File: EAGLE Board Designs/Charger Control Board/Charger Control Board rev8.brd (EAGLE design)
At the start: 86.4 x 83.8 mm, 121 parts, among them J1 CONNECTOR-4_μF_T_V_BLACK, K1 RELAY_DPDT_RT424024, K2 RELAY_DPDT_RT424024, K3 RELAY_DPDT_RT424024, U1 LOGICGATE_BUFFER, U2 ADM8316WBX30, U3 VOLTAGE_REGULATOR_MODULE_OKI-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, U4 TCAN1051HQV-Q1, U5 TCAN1051HQV-Q1

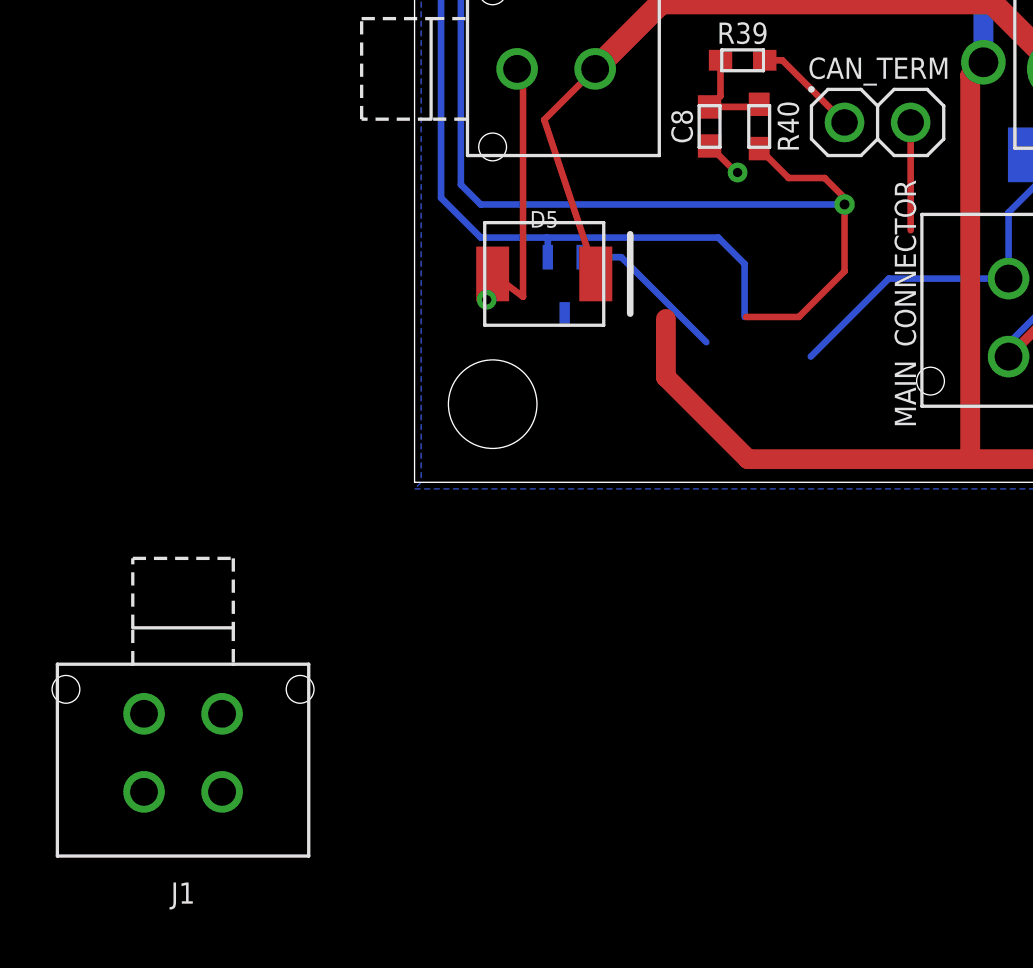
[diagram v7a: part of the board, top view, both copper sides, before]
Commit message: positioning of J1
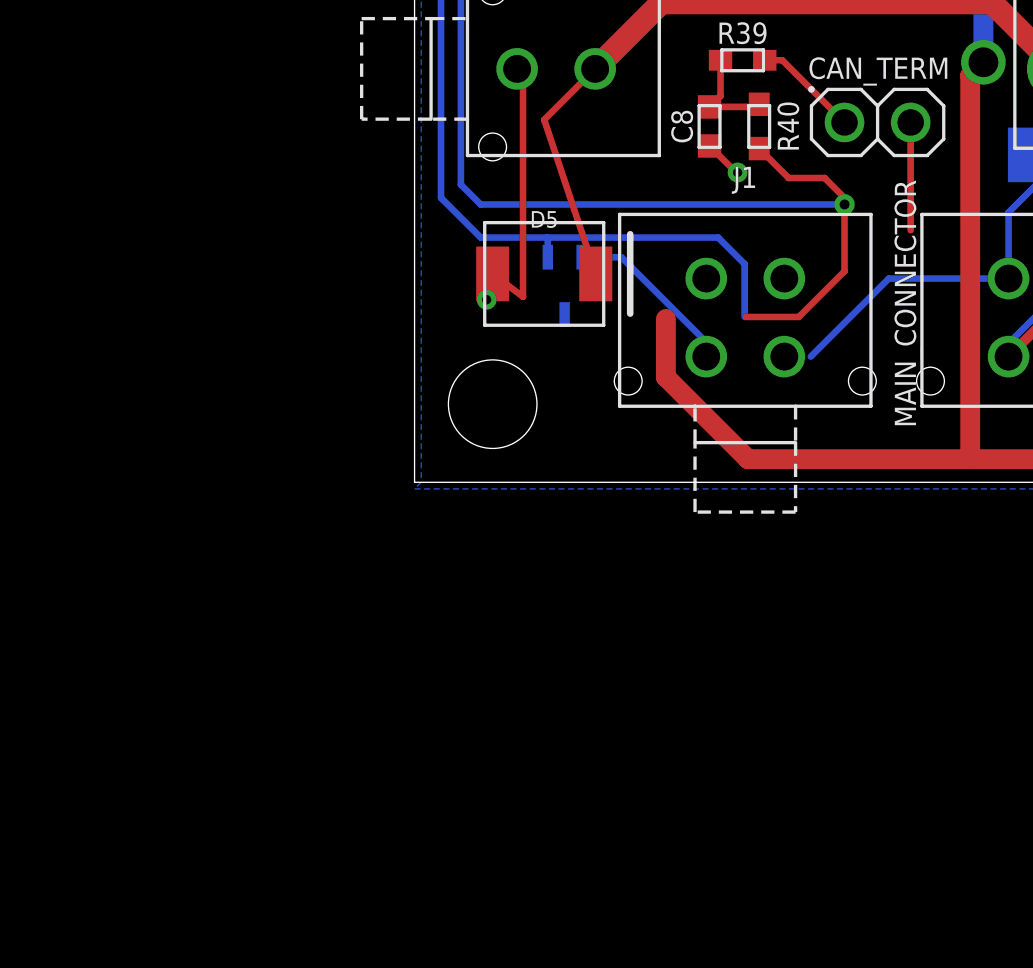
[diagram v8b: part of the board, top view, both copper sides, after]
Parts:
- moved J1 25.6 mm to (12.7, 4.83), turned to 180 degrees
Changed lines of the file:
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@@
 <attribute name="NAME" x="16.383" y="73.787" size="0.8128" layer="25" font="vector" rot="R90" align="bottom-center"/>
 </element>
-<element name="J1" library="HyTechDevices" package="MOLEX_MICROFIT_PTH_VERTICAL_04_DUAL" value="CONNECTOR-4_μF_T_V_BLACK" x="-8.89" y="-8.89" smashed="yes">
-<attribute name="DKPN" value="2266-43045-0414-ND" x="-8.89" y="-8.89" size="1.778" layer="27" display="off"/>
-<attribute name="MANUFACTURER" value="Molex" x="-8.89" y="-8.89" size="1.778" layer="27" display="off"/>
-<attribute name="MOPN" value="538-43045-0414" x="-8.89" y="-8.89" size="1.778" layer="27" display="off"/>
-<attribute name="MPN" value="430450414" x="-8.89" y="-8.89" size="1.778" layer="27" display="off"/>
-<attribute name="NAME" x="-8.89" y="-15.367" size="0.8128" layer="25" rot="R180" align="bottom-center"/>
+<element name="J1" library="HyTechDevices" package="MOLEX_MICROFIT_PTH_VERTICAL_04_DUAL" value="CONNECTOR-4_μF_T_V_BLACK" x="12.7" y="4.826" smashed="yes" rot="R180">
+<attribute name="DKPN" value="2266-43045-0414-ND" x="12.7" y="4.826" size="1.778" layer="27" rot="R180" display="off"/>
+<attribute name="MANUFACTURER" value="Molex" x="12.7" y="4.826" size="1.778" layer="27" rot="R180" display="off"/>
+<attribute name="MOPN" value="538-43045-0414" x="12.7" y="4.826" size="1.778" layer="27" rot="R180" display="off"/>
+<attribute name="MPN" value="430450414" x="12.7" y="4.826" size="1.778" layer="27" rot="R180" display="off"/>
+<attribute name="NAME" x="12.7" y="11.303" size="0.8128" layer="25" align="bottom-center"/>
 </element>
 </elements>
@@
 <wire x1="5.7658" y1="6.4438" x2="2.7686" y2="7.0104" width="0" layer="19" extent="16-16"/>
 <wire x1="11.3284" y1="12.9152" x2="3.937" y2="15.875" width="0" layer="19" extent="1-1"/>
+<wire x1="14.1986" y1="4.826" x2="12.4042875" y2="11.8962875" width="0" layer="19" extent="1-1"/>
 <wire x1="48.9204" y1="48.6918" x2="52.8442" y2="57.277" width="0" layer="19" extent="1-1"/>
 <wire x1="18.022" y1="69.977" x2="8.89" y2="66.04" width="0" layer="19" extent="16-16"/>
-<wire x1="24.13" y1="71.64" x2="18.022" y2="69.977" width="0" layer="19" extent="16-16"/>
+<wire x1="18.923" y1="71.1835" x2="18.022" y2="69.977" width="0" layer="19" extent="1-16"/>
+<wire x1="24.13" y1="71.64" x2="18.923" y2="71.1835" width="0" layer="19" extent="1-16"/>
+<wire x1="17.653" y1="76.3905" x2="18.923" y2="71.1835" width="0" layer="19" extent="1-1"/>
+<wire x1="11.43" y1="81.28" x2="17.653" y2="76.3905" width="0" layer="19" extent="1-1"/>
 <wire x1="23.42" y1="12.573" x2="12.4042875" y2="11.8962875" width="0" layer="19" extent="16-16"/>
 <wire x1="27.23" y1="12.573" x2="23.42" y2="12.573" width="0" layer="19" extent="16-16"/>
@@
 <wire x1="46.0502" y1="4.826" x2="41.0464" y2="13.3252" width="0" layer="19" extent="16-16"/>
 <wire x1="54.9784" y1="3.1094" x2="46.0502" y2="4.826" width="0" layer="19" extent="1-1"/>
-<wire x1="11.43" y1="81.28" x2="18.022" y2="69.977" width="0" layer="19" extent="16-16"/>
 <wire x1="79.97" y1="34.23" x2="79.97" y2="47.692" width="0" layer="19" extent="1-1"/>
 <wire x1="79.97" y1="20.768" x2="79.97" y2="34.23" width="0" layer="19" extent="1-1"/>
-<wire x1="17.653" y1="76.3905" x2="2.7686" y2="7.0104" width="0" layer="19" extent="1-1"/>
-<wire x1="18.923" y1="71.1835" x2="17.653" y2="76.3905" width="0" layer="19" extent="1-1"/>
-<wire x1="-10.3886" y1="-8.89" x2="17.653" y2="76.3905" width="0" layer="19" extent="1-1"/>
 <wire x1="44.45" y1="81.28" x2="44.9208" y2="59.817" width="0" layer="19" extent="1-1"/>
 </signal>
@@
 <wire x1="39.9386" y1="32.766" x2="37.465" y2="32.766" width="0.381" layer="1"/>
 <contactref element="J1" pad="1"/>
-<wire x1="9.652" y1="6.2738" x2="-7.3914" y2="-11.8872" width="0" layer="19" extent="1-1"/>
+<wire x1="9.652" y1="6.2738" x2="11.2014" y2="7.8232" width="0" layer="19" extent="1-1"/>
 </signal>
 <signal name="+5V">
@@
 <contactref element="U5" pad="6"/>
 <contactref element="J1" pad="3"/>
-<wire x1="15.113" y1="52.959" x2="22.1615" y2="52.959" width="0" layer="19" extent="1-16"/>
+<wire x1="8.2042" y1="73.152" x2="20.193" y2="76.3905" width="0" layer="19" extent="1-16"/>
 <wire x1="11.2014" y1="5.3822" x2="12.7254" y2="6.35" width="0" layer="19" extent="1-16"/>
-<wire x1="15.0518" y1="0.9756" x2="12.7254" y2="6.35" width="0" layer="19" extent="1-16"/>
-<wire x1="20.193" y1="76.3905" x2="15.0518" y2="0.9756" width="0" layer="19" extent="1-16"/>
-<wire x1="-7.3914" y1="-8.89" x2="20.193" y2="76.3905" width="0" layer="19" extent="1-1"/>
+<wire x1="11.2014" y1="4.826" x2="11.2014" y2="5.3822" width="0" layer="19" extent="16-16"/>
+<wire x1="15.0518" y1="0.9756" x2="11.2014" y2="4.826" width="0" layer="19" extent="16-16"/>
+<wire x1="22.1615" y1="52.959" x2="15.113" y2="52.959" width="0" layer="19" extent="1-16"/>
 </signal>
 <signal name="CANH">
@@
 <contactref element="U5" pad="7"/>
 <contactref element="J1" pad="2"/>
-<wire x1="16.8275" y1="54.356" x2="22.1615" y2="54.229" width="0" layer="19" extent="1-16"/>
+<wire x1="8.382" y1="74.422" x2="18.923" y2="76.3905" width="0" layer="19" extent="1-16"/>
+<wire x1="14.1986" y1="7.8232" x2="12.6746" y2="6.35" width="0" layer="19" extent="16-16"/>
 <wire x1="15.2146" y1="4.826" x2="12.6746" y2="6.35" width="0" layer="19" extent="16-16"/>
 <wire x1="19.05" y1="9.6774" x2="22.8092" y2="7.8232" width="0" layer="19" extent="1-1"/>
-<wire x1="18.923" y1="76.3905" x2="5.1158" y2="8.6438" width="0" layer="19" extent="1-16"/>
-<wire x1="-10.3886" y1="-11.8872" x2="18.923" y2="76.3905" width="0" layer="19" extent="1-1"/>
+<wire x1="22.1615" y1="54.229" x2="16.8275" y2="54.356" width="0" layer="19" extent="1-16"/>
 </signal>
 <signal name="+3V3">
